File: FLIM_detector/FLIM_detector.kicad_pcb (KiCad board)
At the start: 2 copper layers, 23.8 x 21.8 mm, 18 parts, among them J1 Conn_01x02_Female, J2 Conn_01x02_Female, U1 AMS1117-5.0, U2 OPA858xDSG, U3 LM4040DBZ-2.0

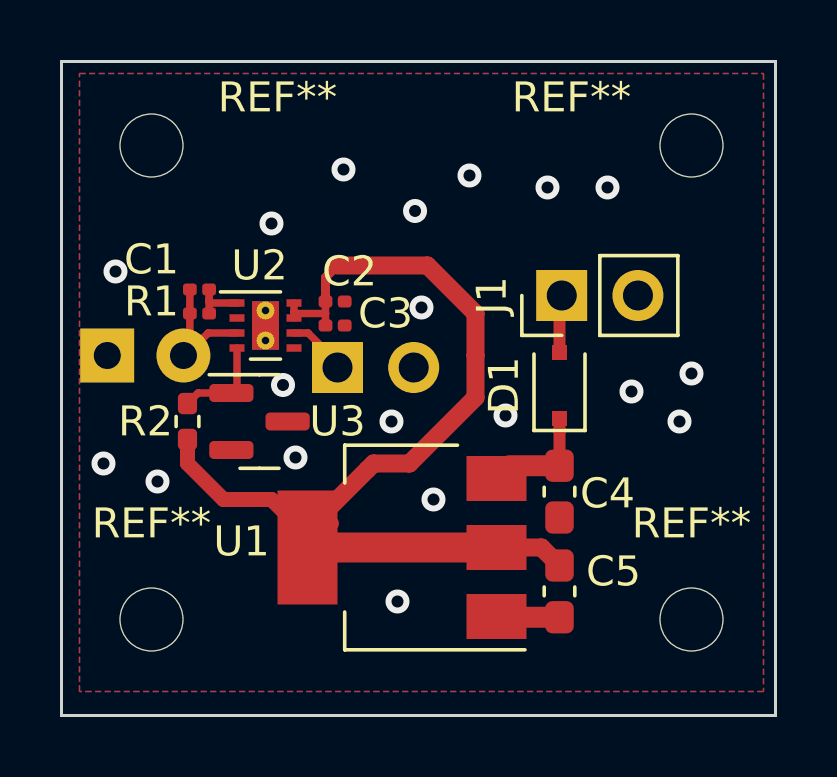
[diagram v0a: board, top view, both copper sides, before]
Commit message: v0.92 silk was corrected
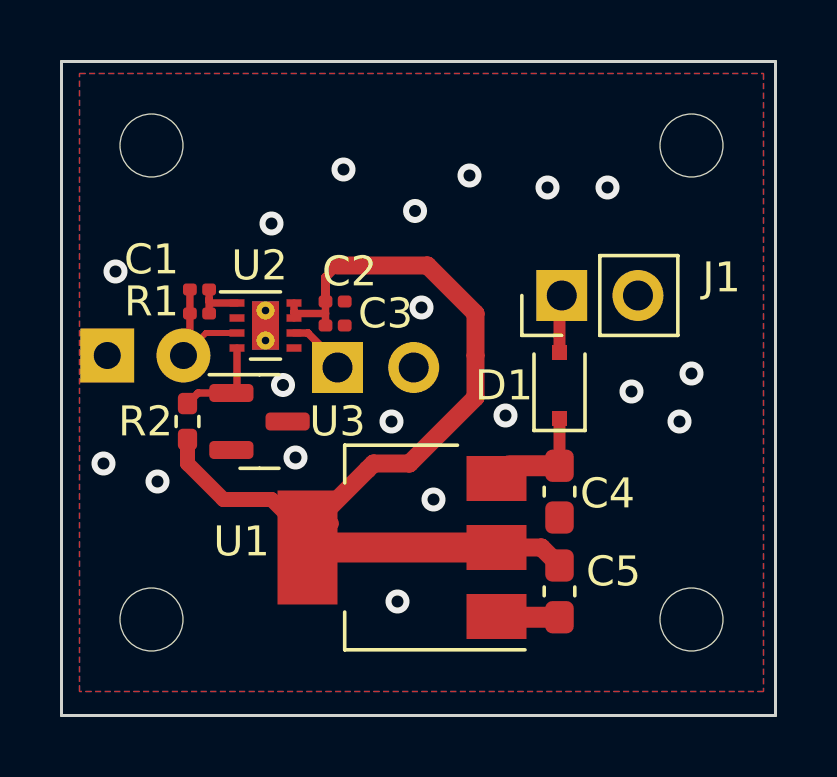
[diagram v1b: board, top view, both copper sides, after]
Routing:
- net Net-(U2-Pad3): track 3.76 -> 4.38 mm
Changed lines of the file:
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@@
     (tags "mounting hole 2.1mm no annular")
     (attr exclude_from_pos_files exclude_from_bom)
-    (fp_text reference "REF**" (at 4.2 -1.6) (layer "F.SilkS")
+    (fp_text reference "REF**" (at 4.2 -1.6) (layer "F.SilkS") hide
       (effects (font (size 1 1) (thickness 0.15)))
     )
@@
     (property "Sheetname" "")
     (attr through_hole)
-    (fp_text reference "J1" (at 0 -2.33 90) (layer "F.SilkS")
+    (fp_text reference "J1" (at 0.6 5.325 180) (layer "F.SilkS")
       (effects (font (size 1 1) (thickness 0.15)))
     )
@@
     (tags "mounting hole 2.1mm no annular")
     (attr exclude_from_pos_files exclude_from_bom)
-    (fp_text reference "REF**" (at 0 -3.2) (layer "F.SilkS")
+    (fp_text reference "REF**" (at 0 -3.2) (layer "F.SilkS") hide
       (effects (font (size 1 1) (thickness 0.15)))
     )
@@
     (property "Sheetname" "")
     (attr smd)
-    (fp_text reference "D1" (at 0 -1.85 90) (layer "F.SilkS")
+    (fp_text reference "D1" (at 0 -1.85 180) (layer "F.SilkS")
       (effects (font (size 1 1) (thickness 0.15)))
     )
@@
     (tags "mounting hole 2.1mm no annular")
     (attr exclude_from_pos_files exclude_from_bom)
-    (fp_text reference "REF**" (at 0 -3.2) (layer "F.SilkS")
+    (fp_text reference "REF**" (at 0 -3.2) (layer "F.SilkS") hide
       (effects (font (size 1 1) (thickness 0.15)))
     )
@@
     (tags "mounting hole 2.1mm no annular")
     (attr exclude_from_pos_files exclude_from_bom)
-    (fp_text reference "REF**" (at -4 -1.6) (layer "F.SilkS")
+    (fp_text reference "REF**" (at -4 -1.6) (layer "F.SilkS") hide
       (effects (font (size 1 1) (thickness 0.15)))
     )
@@
   (segment (start 259 43.4) (end 257.4 41.8) (width 0.6) (layer "F.Cu") (net 3))
   (segment (start 249.4 47.5975) (end 249.4 48.4) (width 0.5) (layer "F.Cu") (net 3))
-  (segment (start 253.419639 44.05) (end 254.569639 45.2) (width 0.25) (layer "F.Cu") (net 4))
+  (segment (start 254.4 45.039022) (end 254.4 45.2) (width 0.25) (layer "F.Cu") (net 4))
   (segment (start 252.95 44.05) (end 253.419639 44.05) (width 0.25) (layer "F.Cu") (net 4))
+  (segment (start 253.419639 44.058661) (end 254.4 45.039022) (width 0.25) (layer "F.Cu") (net 4))
+  (segment (start 253.419639 44.05) (end 253.419639 44.058661) (width 0.25) (layer "F.Cu") (net 4))
   (segment (start 254.569639 45.2) (end 254.725 45.2) (width 0.25) (layer "F.Cu") (net 4))
   (segment (start 261.8 48.475) (end 260.125 48.475) (width 0.7) (layer "F.Cu") (net 5))
@@
   (segment (start 261.8 42.875) (end 261.875 42.8) (width 0.25) (layer "F.Cu") (net 6))
   (segment (start 249.48 42.6) (end 249.48 43.4) (width 0.25) (layer "F.Cu") (net 8))
-  (segment (start 249.54 44.6) (end 249.48 44.54) (width 0.25) (layer "F.Cu") (net 8))
-  (segment (start 251.05 44.05) (end 250.09 44.05) (width 0.25) (layer "F.Cu") (net 8))
-  (segment (start 250.09 44.05) (end 249.54 44.6) (width 0.25) (layer "F.Cu") (net 8))
-  (segment (start 249.48 44.54) (end 249.48 43.4) (width 0.25) (layer "F.Cu") (net 8))
+  (segment (start 250.015 44.05) (end 249.265 44.8) (width 0.2) (layer "F.Cu") (net 8))
+  (segment (start 249.48 43.4) (end 249.48 44.585) (width 0.25) (layer "F.Cu") (net 8))
+  (segment (start 251.05 44.05) (end 250.015 44.05) (width 0.2) (layer "F.Cu") (net 8))
+  (segment (start 249.48 44.585) (end 249.265 44.8) (width 0.25) (layer "F.Cu") (net 8))
   (segment (start 251.05 45.8625) (end 250.8625 46.05) (width 0.25) (layer "F.Cu") (net 9))
   (segment (start 251.05 44.55) (end 251.05 45.8625) (width 0.25) (layer "F.Cu") (net 9))
